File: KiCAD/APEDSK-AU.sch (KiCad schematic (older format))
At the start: 26 parts, among them J1 240-44-44Pins, P1 Power, P2 Analog, P3 Digital, P4 Digital, U1 74LS245, U2 74LS541, U3 74LS541, U4 74LS138, U5 74HC595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

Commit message: R1, MBE
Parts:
- removed R2: 5.1K, Resistor_THT:R_Axial_DIN0204_L3.6mm_D1.6mm_P5.08mm_Horizontal, symbol Device:R_Small_US
- renumbered R3 to R2, R4 to R3, R5 to R4, R6 to R5
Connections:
- net GND: no longer U3.7 (A5)
- net ~AD_WE: no longer U1.19 (CE)
- net ~MBE: now also U3.7 (A5)
- net CE_245: now reaches U3.13 (Y5)
- net CE_245: now also U1.19 (CE)
- no-connect marks 41 -> 39
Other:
- moved on the sheet: R1
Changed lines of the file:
@@
 EESchema Schematic File Version 4
+LIBS:APEDSK-AU-cache
 EELAYER 29 0
 EELAYER END
@@
 Text Label 3000 6200 0    50   ~ 0
 AD_A10
-Text Label 2000 6600 2    50   ~ 0
+Text Label 1800 6500 2    50   ~ 0
 ~MBE
 Text Label 2000 6700 2    50   ~ 0
@@
 $Comp
 L Device:R_Small_US R2
-U 1 1 5D2D397E
-P 6750 3050
-F 0 "R2" H 6818 3096 50  0000 L CNN
-F 1 "5.1K" H 6818 3005 50  0000 L CNN
-F 2 "Resistor_THT:R_Axial_DIN0204_L3.6mm_D1.6mm_P5.08mm_Horizontal" H 6750 3050 50  0001 C CNN
-F 3 "~" H 6750 3050 50  0001 C CNN
-	1    6750 3050
-	1    0    0    -1
-$EndComp
-$Comp
-L Device:R_Small_US R3
 U 1 1 5D2D3984
 P 8700 3350
-F 0 "R3" H 8768 3396 50  0000 L CNN
+F 0 "R2" H 8768 3396 50  0000 L CNN
 F 1 "5.1K" H 8768 3305 50  0000 L CNN
 F 2 "Resistor_THT:R_Axial_DIN0204_L3.6mm_D1.6mm_P5.08mm_Horizontal" H 8700 3350 50  0001 C CNN
@@
 $EndComp
 $Comp
-L Device:R_Small_US R4
+L Device:R_Small_US R3
 U 1 1 5D2D398A
 P 9000 3450
-F 0 "R4" H 9068 3496 50  0000 L CNN
+F 0 "R3" H 9068 3496 50  0000 L CNN
 F 1 "5.1K" H 9068 3405 50  0000 L CNN
 F 2 "Resistor_THT:R_Axial_DIN0204_L3.6mm_D1.6mm_P5.08mm_Horizontal" H 9000 3450 50  0001 C CNN
@@
 $EndComp
 $Comp
-L Device:R_Small_US R5
+L Device:R_Small_US R4
 U 1 1 5D2D3990
 P 9300 3450
-F 0 "R5" H 9368 3496 50  0000 L CNN
+F 0 "R4" H 9368 3496 50  0000 L CNN
 F 1 "5.1K" H 9368 3405 50  0000 L CNN
 F 2 "Resistor_THT:R_Axial_DIN0204_L3.6mm_D1.6mm_P5.08mm_Horizontal" H 9300 3450 50  0001 C CNN
@@
 $EndComp
 $Comp
-L Device:R_Small_US R6
+L Device:R_Small_US R5
 U 1 1 5D2D399D
 P 9650 3350
-F 0 "R6" H 9718 3396 50  0000 L CNN
+F 0 "R5" H 9718 3396 50  0000 L CNN
 F 1 "68R" H 9718 3305 50  0000 L CNN
 F 2 "Resistor_THT:R_Axial_DIN0204_L3.6mm_D1.6mm_P5.08mm_Horizontal" H 9650 3350 50  0001 C CNN
@@
 	-1   0    0    -1
 $EndComp
-Wire Wire Line
-	7350 3150 6750 3150
-$Comp
-L power:+5V #PWR0115
-U 1 1 5D2D39B9
-P 6750 2950
-F 0 "#PWR0115" H 6750 2800 50  0001 C CNN
-F 1 "+5V" H 6765 3123 50  0000 C CNN
-F 2 "" H 6750 2950 50  0001 C CNN
-F 3 "" H 6750 2950 50  0001 C CNN
-	1    6750 2950
-	-1   0    0    -1
-$EndComp
 $Comp
 L Device:R_Small_US R1
 U 1 1 5D2D39BF
-P 6550 3150
-F 0 "R1" V 6345 3150 50  0000 C CNN
-F 1 "1K" V 6436 3150 50  0000 C CNN
-F 2 "Resistor_THT:R_Axial_DIN0204_L3.6mm_D1.6mm_P5.08mm_Horizontal" H 6550 3150 50  0001 C CNN
-F 3 "~" H 6550 3150 50  0001 C CNN
-	1    6550 3150
+P 6800 3150
+F 0 "R1" V 6595 3150 50  0000 C CNN
+F 1 "1K" V 6686 3150 50  0000 C CNN
+F 2 "Resistor_THT:R_Axial_DIN0204_L3.6mm_D1.6mm_P5.08mm_Horizontal" H 6800 3150 50  0001 C CNN
+F 3 "~" H 6800 3150 50  0001 C CNN
+	1    6800 3150
 	0    1    1    0
 $EndComp
-Wire Wire Line
-	6650 3150 6750 3150
-Connection ~ 6750 3150
-Text Label 6450 3150 2    50   ~ 0
+Text Label 6700 3150 2    50   ~ 0
 READY
 NoConn ~ 4800 6950
@@
 NoConn ~ 1350 3600
 NoConn ~ 1350 4100
-NoConn ~ 3100 6450
-NoConn ~ 3000 6500
 Wire Wire Line
 	3000 6600 3450 6600
@@
 AD_A0
 Wire Wire Line
-	2000 6500 1700 6500
-$Comp
-L power:GND #PWR0132
-U 1 1 5D4DF201
-P 1700 6500
-F 0 "#PWR0132" H 1700 6250 50  0001 C CNN
-F 1 "GND" H 1705 6327 50  0000 C CNN
-F 2 "" H 1700 6500 50  0001 C CNN
-F 3 "" H 1700 6500 50  0001 C CNN
-	1    1700 6500
-	-1   0    0    1
-$EndComp
-Wire Wire Line
 	9000 3250 9150 3250
 Connection ~ 9150 3250
 Wire Wire Line
 	9150 3250 9300 3250
+Wire Wire Line
+	2000 6500 2000 6600
+Wire Wire Line
+	2000 6500 1800 6500
+Connection ~ 2000 6500
+Text Label 3000 6500 0    50   ~ 0
+CE_245
 Text Label 4600 2250 0    50   ~ 0
-~AD_WE
+CE_245
+Wire Wire Line
+	6900 3150 7350 3150
 $EndSCHEMATC

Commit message: update
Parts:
- removed R1: 1K, Resistor_THT:R_Axial_DIN0204_L3.6mm_D1.6mm_P5.08mm_Horizontal, symbol Device:R_Small_US
- added D2: 1N5711, Diode_THT:D_A-405_P5.08mm_Vertical_AnodeUp, symbol Device:D_Schottky_Small
- renumbered R2 to R1, R3 to R2, R4 to R3, R5 to R4
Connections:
- net AD_D0: now also P4.8 (Pin_8); no longer P4.7 (Pin_7)
- net AD_D1: now also P4.7 (Pin_7); no longer P4.5 (Pin_5)
- net CLOCK: now also P2.4 (Pin_4); no longer P2.6 (Pin_6)
- net DS: now also P2.6 (Pin_6); no longer P2.4 (Pin_4)
- net READY: now also D2.2 (A)
- net ~AR_BUF: now also P4.5 (Pin_5), D2.1 (K); no longer P4.8 (Pin_8)
- net TI_INT renamed ~TI_INT
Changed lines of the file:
@@
 Text Label 7350 3550 2    50   ~ 0
 AD_D2
-Text Label 7350 3450 2    50   ~ 0
+Text Label 7350 3250 2    50   ~ 0
 AD_D1
-Text Label 7350 3250 2    50   ~ 0
+Text Label 7350 3150 2    50   ~ 0
 AD_D0
 Text Label 8150 3550 0    50   ~ 0
@@
 Text Label 8150 3450 0    50   ~ 0
 ~AD_WE
-Text Label 8150 3350 0    50   ~ 0
+Text Label 8150 3150 0    50   ~ 0
 DS
 Text Label 8150 3250 0    50   ~ 0
 LATCH
-Text Label 8150 3150 0    50   ~ 0
+Text Label 8150 3350 0    50   ~ 0
 CLOCK
 $Comp
@@
 	3450 6050 4000 6050
 Text Label 7350 3350 2    50   ~ 0
-TI_INT
+~TI_INT
 Wire Wire Line
 	4850 4200 5300 4200
@@
 Text Label 2000 6950 2    50   ~ 0
 ~TIBUF
-Text Label 7350 3150 2    50   ~ 0
+Text Label 7350 3450 2    50   ~ 0
 ~AR_BUF
 $Comp
-L Device:R_Small_US R2
+L Device:R_Small_US R1
 U 1 1 5D2D3984
 P 8700 3350
-F 0 "R2" H 8768 3396 50  0000 L CNN
+F 0 "R1" H 8768 3396 50  0000 L CNN
 F 1 "5.1K" H 8768 3305 50  0000 L CNN
 F 2 "Resistor_THT:R_Axial_DIN0204_L3.6mm_D1.6mm_P5.08mm_Horizontal" H 8700 3350 50  0001 C CNN
@@
 $EndComp
 $Comp
-L Device:R_Small_US R3
+L Device:R_Small_US R2
 U 1 1 5D2D398A
 P 9000 3450
-F 0 "R3" H 9068 3496 50  0000 L CNN
+F 0 "R2" H 9068 3496 50  0000 L CNN
 F 1 "5.1K" H 9068 3405 50  0000 L CNN
 F 2 "Resistor_THT:R_Axial_DIN0204_L3.6mm_D1.6mm_P5.08mm_Horizontal" H 9000 3450 50  0001 C CNN
@@
 $EndComp
 $Comp
-L Device:R_Small_US R4
+L Device:R_Small_US R3
 U 1 1 5D2D3990
 P 9300 3450
-F 0 "R4" H 9368 3496 50  0000 L CNN
+F 0 "R3" H 9368 3496 50  0000 L CNN
 F 1 "5.1K" H 9368 3405 50  0000 L CNN
 F 2 "Resistor_THT:R_Axial_DIN0204_L3.6mm_D1.6mm_P5.08mm_Horizontal" H 9300 3450 50  0001 C CNN
@@
 $EndComp
 $Comp
-L Device:R_Small_US R5
+L Device:R_Small_US R4
 U 1 1 5D2D399D
 P 9650 3350
-F 0 "R5" H 9718 3396 50  0000 L CNN
+F 0 "R4" H 9718 3396 50  0000 L CNN
 F 1 "68R" H 9718 3305 50  0000 L CNN
 F 2 "Resistor_THT:R_Axial_DIN0204_L3.6mm_D1.6mm_P5.08mm_Horizontal" H 9650 3350 50  0001 C CNN
@@
 	-1   0    0    -1
 $EndComp
-$Comp
-L Device:R_Small_US R1
-U 1 1 5D2D39BF
-P 6800 3150
-F 0 "R1" V 6595 3150 50  0000 C CNN
-F 1 "1K" V 6686 3150 50  0000 C CNN
-F 2 "Resistor_THT:R_Axial_DIN0204_L3.6mm_D1.6mm_P5.08mm_Horizontal" H 6800 3150 50  0001 C CNN
-F 3 "~" H 6800 3150 50  0001 C CNN
-	1    6800 3150
-	0    1    1    0
-$EndComp
-Text Label 6700 3150 2    50   ~ 0
+Text Label 6600 3450 2    50   ~ 0
 READY
 NoConn ~ 4800 6950
@@
 NoConn ~ 8150 4450
 NoConn ~ 8150 3850
-Wire Wire Line
-	6800 6250 6800 3350
-Wire Wire Line
-	6800 3350 7350 3350
 $Comp
 L power:GND #PWR0122
@@
 CE_245
 Wire Wire Line
-	6900 3150 7350 3150
+	6900 3450 7350 3450
+$Comp
+L Device:D_Schottky_Small D2
+U 1 1 5E37422E
+P 6800 3450
+F 0 "D2" H 6800 3655 50  0000 C CNN
+F 1 "1N5711" H 6800 3564 50  0000 C CNN
+F 2 "Diode_THT:D_A-405_P5.08mm_Vertical_AnodeUp" V 6800 3450 50  0001 C CNN
+F 3 "~" V 6800 3450 50  0001 C CNN
+	1    6800 3450
+	-1   0    0    -1
+$EndComp
+Wire Wire Line
+	6600 3450 6700 3450
+Wire Wire Line
+	7350 3350 7050 3350
+Wire Wire Line
+	7050 3350 7050 3050
+Wire Wire Line
+	7050 3050 6100 3050
+Wire Wire Line
+	6100 3050 6100 5250
+Wire Wire Line
+	6100 5250 6800 5250
+Wire Wire Line
+	6800 5250 6800 6250
 $EndSCHEMATC

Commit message: update
update
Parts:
- R1: footprint Resistor_THT:R_Axial_DIN0204_L3.6mm_D1.6mm_P5.08mm_Horizontal -> Resistor_THT:R_Axial_DIN0204_L3.6mm_D1.6mm_P5.08mm_Vertical
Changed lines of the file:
@@
 F 0 "R1" H 8768 3396 50  0000 L CNN
 F 1 "5.1K" H 8768 3305 50  0000 L CNN
-F 2 "Resistor_THT:R_Axial_DIN0204_L3.6mm_D1.6mm_P5.08mm_Horizontal" H 8700 3350 50  0001 C CNN
+F 2 "Resistor_THT:R_Axial_DIN0204_L3.6mm_D1.6mm_P5.08mm_Vertical" H 8700 3350 50  0001 C CNN
 F 3 "~" H 8700 3350 50  0001 C CNN
 	1    8700 3350

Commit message: update
update
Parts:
- R2, R3, R4: footprint Resistor_THT:R_Axial_DIN0204_L3.6mm_D1.6mm_P5.08mm_Horizontal -> Resistor_THT:R_Axial_DIN0204_L3.6mm_D1.6mm_P5.08mm_Vertical
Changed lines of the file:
@@
 F 0 "R2" H 9068 3496 50  0000 L CNN
 F 1 "5.1K" H 9068 3405 50  0000 L CNN
-F 2 "Resistor_THT:R_Axial_DIN0204_L3.6mm_D1.6mm_P5.08mm_Horizontal" H 9000 3450 50  0001 C CNN
+F 2 "Resistor_THT:R_Axial_DIN0204_L3.6mm_D1.6mm_P5.08mm_Vertical" H 9000 3450 50  0001 C CNN
 F 3 "~" H 9000 3450 50  0001 C CNN
 	1    9000 3450
@@
 F 0 "R3" H 9368 3496 50  0000 L CNN
 F 1 "5.1K" H 9368 3405 50  0000 L CNN
-F 2 "Resistor_THT:R_Axial_DIN0204_L3.6mm_D1.6mm_P5.08mm_Horizontal" H 9300 3450 50  0001 C CNN
+F 2 "Resistor_THT:R_Axial_DIN0204_L3.6mm_D1.6mm_P5.08mm_Vertical" H 9300 3450 50  0001 C CNN
 F 3 "~" H 9300 3450 50  0001 C CNN
 	1    9300 3450
@@
 F 0 "R4" H 9718 3396 50  0000 L CNN
 F 1 "68R" H 9718 3305 50  0000 L CNN
-F 2 "Resistor_THT:R_Axial_DIN0204_L3.6mm_D1.6mm_P5.08mm_Horizontal" H 9650 3350 50  0001 C CNN
+F 2 "Resistor_THT:R_Axial_DIN0204_L3.6mm_D1.6mm_P5.08mm_Vertical" H 9650 3350 50  0001 C CNN
 F 3 "~" H 9650 3350 50  0001 C CNN
 	1    9650 3350

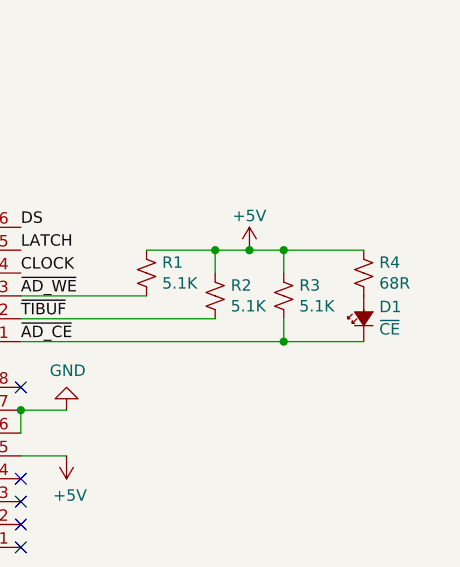
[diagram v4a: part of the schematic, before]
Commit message: update R4 value
R4 value
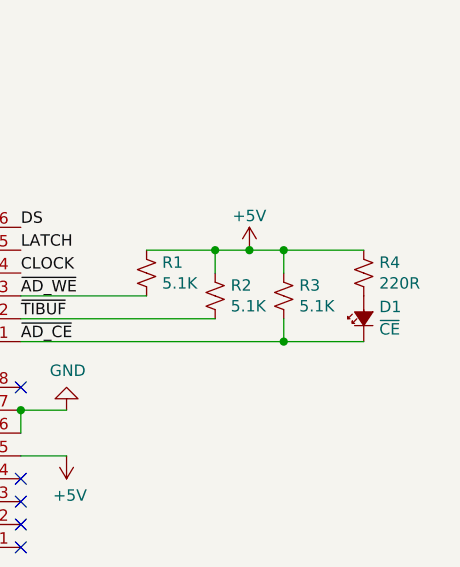
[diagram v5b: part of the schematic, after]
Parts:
- R4: value 68R -> 220R
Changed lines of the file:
@@
 P 9650 3350
 F 0 "R4" H 9718 3396 50  0000 L CNN
-F 1 "68R" H 9718 3305 50  0000 L CNN
+F 1 "220R" H 9718 3305 50  0000 L CNN
 F 2 "Resistor_THT:R_Axial_DIN0204_L3.6mm_D1.6mm_P5.08mm_Vertical" H 9650 3350 50  0001 C CNN
 F 3 "~" H 9650 3350 50  0001 C CNN

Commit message: update
update
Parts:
- R4: value 220R -> 330R
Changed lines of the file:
@@
 	-1   0    0    1
-$EndComp
-$Comp
-L Connector_Generic:Conn_01x08 P4
-U 1 1 56D7164F
-P 7550 3550
-F 0 "P4" H 7550 3050 50  0000 C CNN
-F 1 "Digital" V 7650 3550 50  0000 C CNN
-F 2 "Socket_Arduino_Uno:Socket_Strip_Arduino_1x08" V 7700 3500 20  0000 C CNN
-F 3 "" H 7550 3550 50  0000 C CNN
-	1    7550 3550
-	1    0    0    1
-$EndComp
-$Comp
-L Connector_Generic:Conn_01x10 P3
-U 1 1 56D721E0
-P 7550 4550
-F 0 "P3" H 7550 5100 50  0000 C CNN
-F 1 "Digital" V 7650 4550 50  0000 C CNN
-F 2 "Socket_Arduino_Uno:Socket_Strip_Arduino_1x10" V 7700 4550 20  0000 C CNN
-F 3 "" H 7550 4550 50  0000 C CNN
-	1    7550 4550
-	1    0    0    1
 $EndComp
 Text Notes 7850 4550 2    60   ~ 0
@@
 P 9650 3350
 F 0 "R4" H 9718 3396 50  0000 L CNN
-F 1 "220R" H 9718 3305 50  0000 L CNN
+F 1 "330R" H 9718 3305 50  0000 L CNN
 F 2 "Resistor_THT:R_Axial_DIN0204_L3.6mm_D1.6mm_P5.08mm_Vertical" H 9650 3350 50  0001 C CNN
 F 3 "~" H 9650 3350 50  0001 C CNN
@@
 Wire Wire Line
 	6800 5250 6800 6250
+$Comp
+L Connector_Generic:Conn_01x10 P3
+U 1 1 56D721E0
+P 7550 4550
+F 0 "P3" H 7550 5100 50  0000 C CNN
+F 1 "Digital" V 7650 4550 50  0000 C CNN
+F 2 "Socket_Arduino_Uno:Socket_Strip_Arduino_1x10" V 7700 4550 20  0000 C CNN
+F 3 "" H 7550 4550 50  0000 C CNN
+	1    7550 4550
+	1    0    0    1
+$EndComp
+$Comp
+L Connector_Generic:Conn_01x08 P4
+U 1 1 56D7164F
+P 7550 3550
+F 0 "P4" H 7550 3050 50  0000 C CNN
+F 1 "Digital" V 7650 3550 50  0000 C CNN
+F 2 "Socket_Arduino_Uno:Socket_Strip_Arduino_1x08" V 7700 3500 20  0000 C CNN
+F 3 "" H 7550 3550 50  0000 C CNN
+	1    7550 3550
+	1    0    0    1
+$EndComp
 $EndSCHEMATC
